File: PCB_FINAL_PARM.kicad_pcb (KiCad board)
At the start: 2 copper layers, 87.6 x 95.2 mm, 42 parts, among them J1 Conn_01x02_Servo1, J2 Conn_01x03_UART1, J3 Conn_01x03_UART2, J4 Conn_01x04_PWM, J5 Conn_01x05_PROGRAMER, J6 Conn_01x02_POWER, J7 Conn_01x02_Servo2, J8 Conn_01x02_Servo3, J9 Conn_01x02_Servo4, U2 DSPIC33EP128GM604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

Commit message: Proyecto Almost finalizado
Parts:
- added J10: Conn_01x04_TRIS, Connector_PinHeader_2.54mm:PinHeader_1x04_P2.54mm_Vertical, F.Cu at (209.4, 127.6)
- moved G*** 1.90 mm to (152.6, 63.3)
- moved C6 1.78 mm to (182.7, 117.8)
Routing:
- net Net-(J10-Pad1): track 0.00 -> 32.9 mm, vias 0 -> 1
- net Net-(J10-Pad2): track 0.00 -> 30.7 mm, vias 0 -> 1
- net Net-(J10-Pad3): track 0.00 -> 28.5 mm, vias 0 -> 1
- net Net-(J10-Pad4): track 0.00 -> 26.2 mm, vias 0 -> 1
- net Net-(J5-Pad5): track 51.0 -> 68.1 mm
- net Net-(J5-Pad4): track 64.9 -> 80.4 mm
- net GND: track 454.2 -> 455.6 mm
- net Net-(J4-Pad4): track 36.4 -> 37.8 mm
- net Net-(J4-Pad3): track 33.1 -> 34.1 mm
- net Net-(C3-Pad2): track 47.1 -> 46.4 mm
- net Net-(J4-Pad2): track 33.1 -> 33.7 mm
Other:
- board text added: "1"
- board text added: "2"
- board text added: "3"
- board text added: "3.3V"
- board text added: "4"
- board text added: "AUX"
- board text added: "M1"
- board text added: "M2"
- board text added: "M3"
- board text added: "P-ARM X Æ A-12"
- board text added: "RX"
- board text added: "TRIS PORT"
- board text added: "TX"
- board text removed: "P-ARM ALMOST"
- board text removed: "TM"

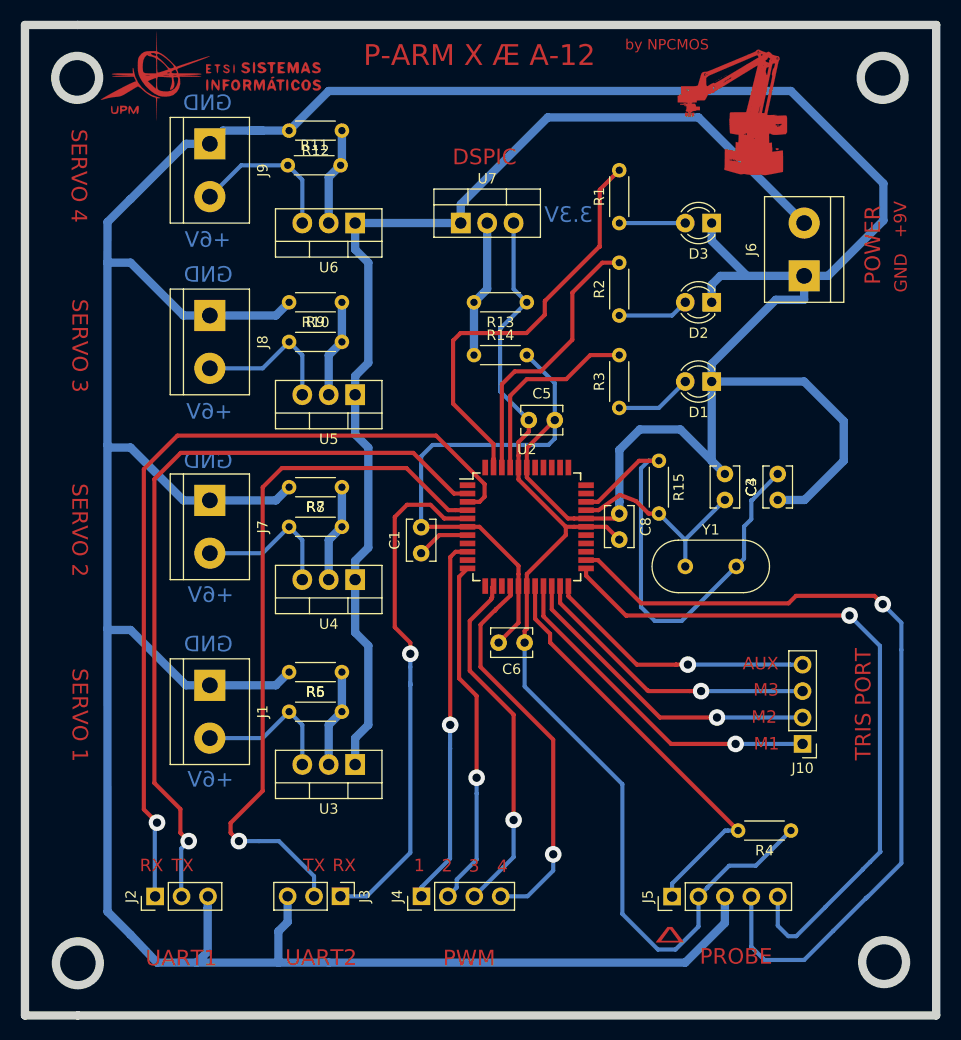
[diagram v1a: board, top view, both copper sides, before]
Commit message: Añadido puerto tris y clema extra
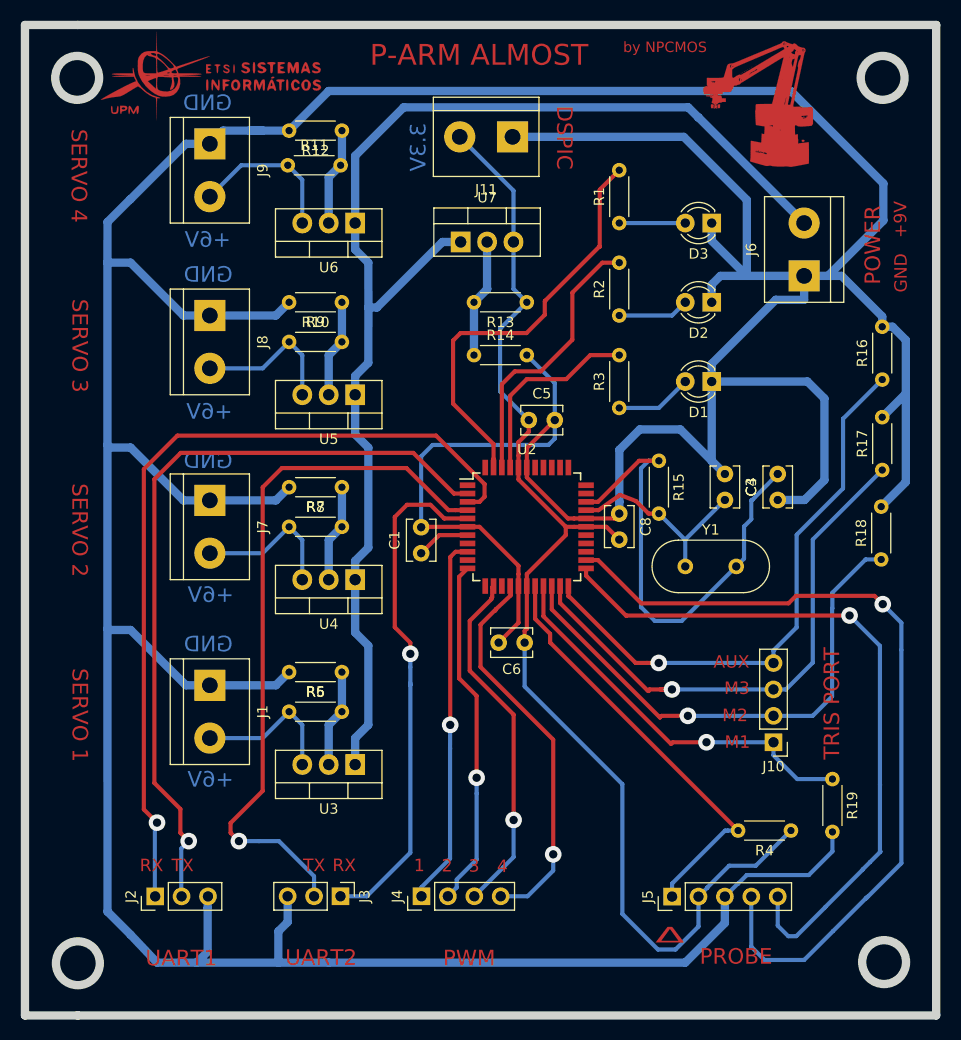
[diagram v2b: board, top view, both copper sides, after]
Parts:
- added J11: Conn_01x02_DSP, TerminalBlock:TerminalBlock_bornier-2_P5.08mm, F.Cu at (181.5, 69.2)
- added R16: 1k, Resistor_THT:R_Axial_DIN0204_L3.6mm_D1.6mm_P5.08mm_Horizontal, F.Cu at (217.1, 92.5)
- added R17: 1k, Resistor_THT:R_Axial_DIN0204_L3.6mm_D1.6mm_P5.08mm_Horizontal, F.Cu at (217.1, 101.2)
- added R18: 1k, Resistor_THT:R_Axial_DIN0204_L3.6mm_D1.6mm_P5.08mm_Horizontal, F.Cu at (217.0, 109.8)
- added R19: 1k, Resistor_THT:R_Axial_DIN0204_L3.6mm_D1.6mm_P5.08mm_Horizontal, F.Cu at (212.3, 130.9)
- moved J10 2.80 mm to (206.6, 127.4)
- moved G*** 2.62 mm to (205.2, 66.2)
- moved U7 1.82 mm to (176.5, 79.3)
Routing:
- net GND: track 455.6 -> 531.5 mm
- net Net-(J10-Pad4): track 26.2 -> 55.0 mm
- net Net-(J10-Pad3): track 28.5 -> 53.0 mm
- net Net-(J10-Pad2): track 30.7 -> 50.4 mm
- net Net-(J6-Pad2): track 107.9 -> 122.9 mm
- net +3V3: track 106.8 -> 117.2 mm
- net Net-(J10-Pad1): track 32.9 -> 38.4 mm
- net Net-(R13-Pad2): track 13.2 -> 11.4 mm
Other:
- board text added: "P-ARM ALMOST"
- board text removed: "P-ARM X Æ A-12"

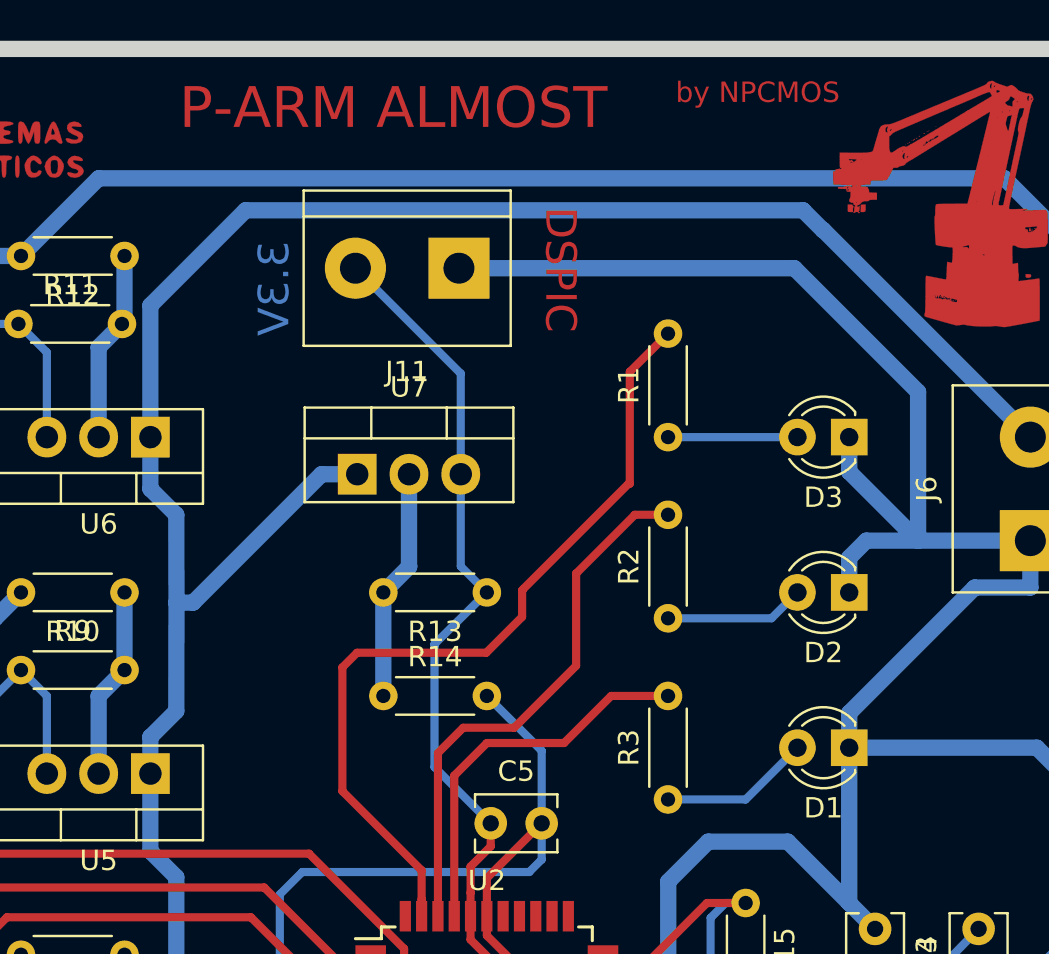
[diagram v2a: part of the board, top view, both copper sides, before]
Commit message: Añadido los circuitos de interruptores y sus pines de alimentación
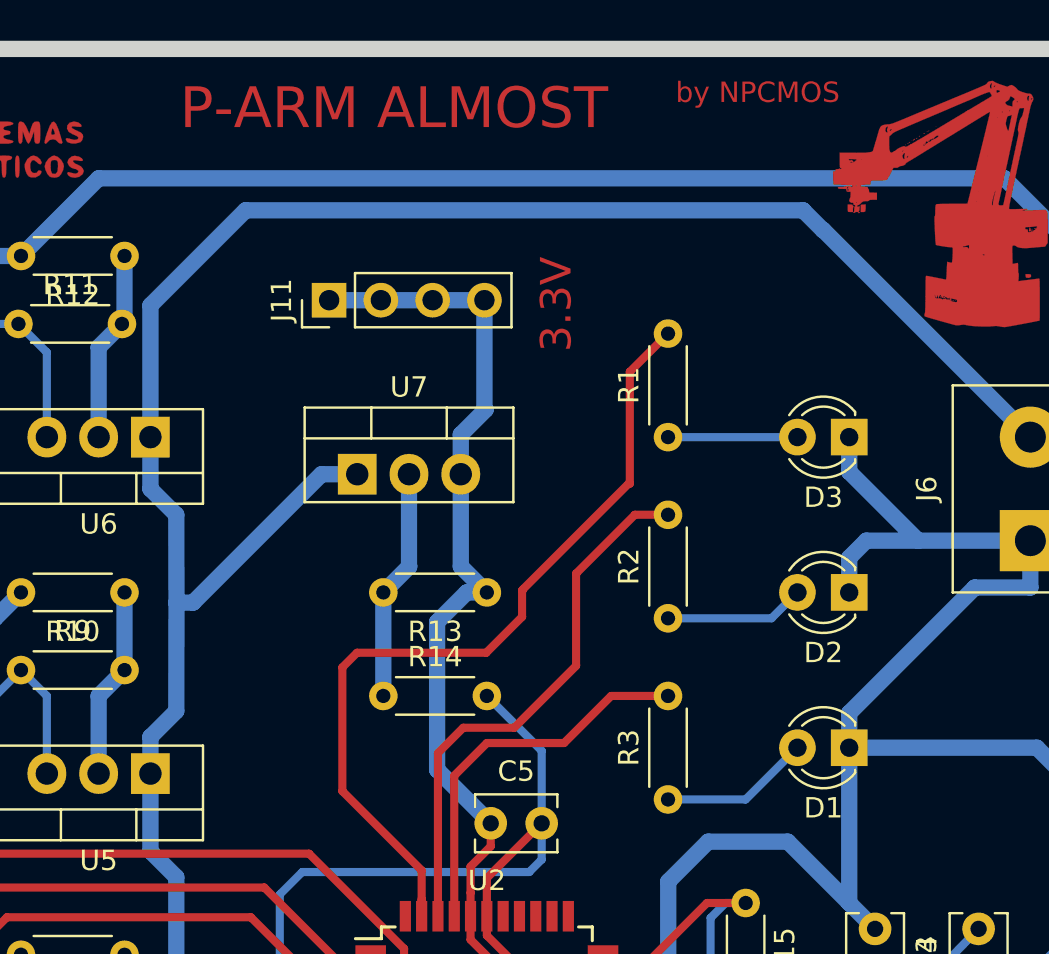
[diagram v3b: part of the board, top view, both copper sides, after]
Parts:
- J11: value Conn_01x02_DSP -> Conn_01x04_3v3; footprint TerminalBlock:TerminalBlock_bornier-2_P5.08mm -> Connector_PinHeader_2.54mm:PinHeader_1x04_P2.54mm_Vertical
- moved J11 6.56 mm to (175.1, 70.8), turned to 90 degrees
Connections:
- J11 pad 1: GND -> +3V3
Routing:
- net GND: track 531.5 -> 499.1 mm
- net +3V3: track 117.2 -> 122.1 mm
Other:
- board text removed: "DSPIC"
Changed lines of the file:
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@@
   (general
     (thickness 1.6)
-    (drawings 47)
-    (tracks 489)
+    (drawings 46)
+    (tracks 492)
     (zones 0)
     (modules 48)
@@
   )
   (setup
-    (last_trace_width 0.4)
+    (last_trace_width 0.8)
     (user_trace_width 0.4)
     (user_trace_width 0.8)
@@
     )
   )
-  (module TerminalBlock:TerminalBlock_bornier-2_P5.08mm (layer F.Cu)
-    (at 181.51 69.18 180)
-    (descr "simple 2-pin terminal block, pitch 5.08mm, revamped version of bornier2")
-    (tags "terminal block bornier2")
-    (fp_text reference J11 (at 2.54 -5.08) (layer F.SilkS)
-      (effects (font (size 1 1) (thickness 0.15)))
-    )
-    (fp_text value Conn_01x02_DSP (at 2.54 5.08) (layer F.Fab)
-      (effects (font (size 1 1) (thickness 0.15)))
-    )
-    (fp_text user %R (at 2.54 0) (layer F.Fab)
-      (effects (font (size 1 1) (thickness 0.15)))
-    )
-    (fp_line (start -2.41 2.55) (end 7.49 2.55) (layer F.Fab) (width 0.1))
-    (fp_line (start -2.46 -3.75) (end -2.46 3.75) (layer F.Fab) (width 0.1))
-    (fp_line (start -2.46 3.75) (end 7.54 3.75) (layer F.Fab) (width 0.1))
-    (fp_line (start 7.54 3.75) (end 7.54 -3.75) (layer F.Fab) (width 0.1))
-    (fp_line (start 7.54 -3.75) (end -2.46 -3.75) (layer F.Fab) (width 0.1))
-    (fp_line (start 7.62 2.54) (end -2.54 2.54) (layer F.SilkS) (width 0.12))
-    (fp_line (start 7.62 3.81) (end 7.62 -3.81) (layer F.SilkS) (width 0.12))
-    (fp_line (start 7.62 -3.81) (end -2.54 -3.81) (layer F.SilkS) (width 0.12))
-    (fp_line (start -2.54 -3.81) (end -2.54 3.81) (layer F.SilkS) (width 0.12))
-    (fp_line (start -2.54 3.81) (end 7.62 3.81) (layer F.SilkS) (width 0.12))
-    (fp_line (start -2.71 -4) (end 7.79 -4) (layer F.CrtYd) (width 0.05))
-    (fp_line (start -2.71 -4) (end -2.71 4) (layer F.CrtYd) (width 0.05))
-    (fp_line (start 7.79 4) (end 7.79 -4) (layer F.CrtYd) (width 0.05))
-    (fp_line (start 7.79 4) (end -2.71 4) (layer F.CrtYd) (width 0.05))
-    (pad 1 thru_hole rect (at 0 0 180) (size 3 3) (drill 1.52) (layers *.Cu *.Mask)
-      (net 2 GND))
-    (pad 2 thru_hole circle (at 5.08 0 180) (size 3 3) (drill 1.52) (layers *.Cu *.Mask)
-      (net 4 +3V3))
-    (model ${KISYS3DMOD}/TerminalBlock.3dshapes/TerminalBlock_bornier-2_P5.08mm.wrl
-      (offset (xyz 2.539999961853027 0 0))
-      (scale (xyz 1 1 1))
-      (rotate (xyz 0 0 0))
-    )
-  )
   (module Resistor_THT:R_Axial_DIN0204_L3.6mm_D1.6mm_P5.08mm_Horizontal (layer F.Cu)
     (at 217.06 92.52 90)
@@
     )
   )
+  (module Connector_PinHeader_2.54mm:PinHeader_1x04_P2.54mm_Vertical (layer F.Cu)
+    (at 175.14 70.75 90)
+    (descr "Through hole straight pin header, 1x04, 2.54mm pitch, single row")
+    (tags "Through hole pin header THT 1x04 2.54mm single row")
+    (fp_text reference J11 (at 0 -2.33 90) (layer F.SilkS)
+      (effects (font (size 1 1) (thickness 0.15)))
+    )
+    (fp_text value Conn_01x04_3v3 (at 0 9.95 90) (layer F.Fab)
+      (effects (font (size 1 1) (thickness 0.15)))
+    )
+    (fp_line (start -0.635 -1.27) (end 1.27 -1.27) (layer F.Fab) (width 0.1))
+    (fp_line (start 1.27 -1.27) (end 1.27 8.89) (layer F.Fab) (width 0.1))
+    (fp_line (start 1.27 8.89) (end -1.27 8.89) (layer F.Fab) (width 0.1))
+    (fp_line (start -1.27 8.89) (end -1.27 -0.635) (layer F.Fab) (width 0.1))
+    (fp_line (start -1.27 -0.635) (end -0.635 -1.27) (layer F.Fab) (width 0.1))
+    (fp_line (start -1.33 8.95) (end 1.33 8.95) (layer F.SilkS) (width 0.12))
+    (fp_line (start -1.33 1.27) (end -1.33 8.95) (layer F.SilkS) (width 0.12))
+    (fp_line (start 1.33 1.27) (end 1.33 8.95) (layer F.SilkS) (width 0.12))
+    (fp_line (start -1.33 1.27) (end 1.33 1.27) (layer F.SilkS) (width 0.12))
+    (fp_line (start -1.33 0) (end -1.33 -1.33) (layer F.SilkS) (width 0.12))
+    (fp_line (start -1.33 -1.33) (end 0 -1.33) (layer F.SilkS) (width 0.12))
+    (fp_line (start -1.8 -1.8) (end -1.8 9.4) (layer F.CrtYd) (width 0.05))
+    (fp_line (start -1.8 9.4) (end 1.8 9.4) (layer F.CrtYd) (width 0.05))
+    (fp_line (start 1.8 9.4) (end 1.8 -1.8) (layer F.CrtYd) (width 0.05))
+    (fp_line (start 1.8 -1.8) (end -1.8 -1.8) (layer F.CrtYd) (width 0.05))
+    (fp_text user %R (at 0 3.81) (layer F.Fab)
+      (effects (font (size 1 1) (thickness 0.15)))
+    )
+    (pad 1 thru_hole rect (at 0 0 90) (size 1.7 1.7) (drill 1) (layers *.Cu *.Mask)
+      (net 4 +3V3))
+    (pad 2 thru_hole oval (at 0 2.54 90) (size 1.7 1.7) (drill 1) (layers *.Cu *.Mask)
+      (net 4 +3V3))
+    (pad 3 thru_hole oval (at 0 5.08 90) (size 1.7 1.7) (drill 1) (layers *.Cu *.Mask)
+      (net 4 +3V3))
+    (pad 4 thru_hole oval (at 0 7.62 90) (size 1.7 1.7) (drill 1) (layers *.Cu *.Mask)
+      (net 4 +3V3))
+    (model ${KISYS3DMOD}/Connector_PinHeader_2.54mm.3dshapes/PinHeader_1x04_P2.54mm_Vertical.wrl
+      (at (xyz 0 0 0))
+      (scale (xyz 1 1 1))
+      (rotate (xyz 0 0 0))
+    )
+  )
+  (gr_text "3.3V\n" (at 186.29 70.95 90) (layer F.Cu)
+    (effects (font (size 1.5 1.5) (thickness 0.3)))
+  )
   (gr_text "TRIS PORT\n" (at 212.22 123.66 90) (layer F.Cu)
     (effects (font (size 1.5 1.5) (thickness 0.3)))
@@
     (effects (font (size 1.2 1.2) (thickness 0.3)))
   )
-  (gr_text 3.3V (at 172.44 70.17 90) (layer B.Cu)
-    (effects (font (size 1.5 1.5) (thickness 0.3)) (justify mirror))
-  )
   (gr_text 4 (at 180.53 139.33) (layer F.Cu)
     (effects (font (size 1.2 1.2) (thickness 0.3)))
@@
   (gr_circle (center 217.24 148.54) (end 219.349502 148.54) (layer Edge.Cuts) (width 0.8))
   (gr_circle (center 217.1 63.509502) (end 219.209502 63.509502) (layer Edge.Cuts) (width 0.8))
-  (gr_text DSPIC (at 186.49 69.25 270) (layer F.Cu)
-    (effects (font (size 1.5 1.5) (thickness 0.3)))
-  )
   (gr_text "SERVO 1" (at 139.89 124.78 270) (layer F.Cu)
     (effects (font (size 1.5 1.5) (thickness 0.3)))
@@
     (effects (font (size 1 1) (thickness 0.125)))
   )
-  (gr_text "P-ARM ALMOST\n\n\n\n" (at 178.29 66.15) (layer F.Cu)
+  (gr_text "P-ARM ALMOST\n\n\n\n" (at 178.32 66.16) (layer F.Cu)
     (effects (font (size 2 2) (thickness 0.3)))
   )
@@
   (segment (start 182.08 115.91) (end 180.17 117.82) (width 0.4) (layer F.Cu) (net 2))
   (segment (start 182.08 112.38) (end 182.08 115.91) (width 0.4) (layer F.Cu) (net 2))
-  (segment (start 181.51 69.18) (end 197.97 69.18) (width 0.8) (layer B.Cu) (net 2))
-  (segment (start 204.04 75.25) (end 204.04 82.55) (width 0.8) (layer B.Cu) (net 2))
-  (segment (start 197.97 69.18) (end 204.04 75.25) (width 0.8) (layer B.Cu) (net 2))
   (segment (start 211.5 102.19) (end 209.59 104.1) (width 0.8) (layer B.Cu) (net 2))
   (segment (start 211.5 94.34) (end 211.5 102.19) (width 0.8) (layer B.Cu) (net 2))
@@
   (segment (start 200.239999 141.390001) (end 200.239999 141.370001) (width 0.4) (layer B.Cu) (net 4))
   (segment (start 200.239999 141.370001) (end 202.34 139.27) (width 0.4) (layer B.Cu) (net 4))
-  (segment (start 183.07 96.42) (end 180.31 93.66) (width 0.4) (layer B.Cu) (net 4))
-  (segment (start 180.31 93.66) (end 180.31 87.63) (width 0.4) (layer B.Cu) (net 4))
-  (segment (start 182.88 85.09) (end 180.31 87.63) (width 0.4) (layer B.Cu) (net 4))
   (segment (start 180.31 87.63) (end 180.34 87.63) (width 0.4) (layer B.Cu) (net 4))
   (segment (start 182.08 99.83) (end 182.08 100.98) (width 0.4) (layer F.Cu) (net 4))
@@
   (segment (start 182.67 122.03) (end 182.67 117.82) (width 0.4) (layer B.Cu) (net 4))
   (segment (start 192.07 131.43) (end 182.67 122.03) (width 0.4) (layer B.Cu) (net 4))
-  (segment (start 181.6 83.81) (end 181.6 79.29) (width 0.4) (layer B.Cu) (net 4))
-  (segment (start 182.88 85.09) (end 181.6 83.81) (width 0.4) (layer B.Cu) (net 4))
-  (segment (start 181.6 74.35) (end 181.6 79.29) (width 0.4) (layer B.Cu) (net 4))
-  (segment (start 176.43 69.18) (end 181.6 74.35) (width 0.4) (layer B.Cu) (net 4))
+  (segment (start 181.6 83.81) (end 182.88 85.09) (width 0.8) (layer B.Cu) (net 4))
+  (segment (start 181.6 79.29) (end 181.6 83.81) (width 0.8) (layer B.Cu) (net 4))
+  (segment (start 181.890051 85.09) (end 180.44 86.540051) (width 0.8) (layer B.Cu) (net 4))
+  (segment (start 182.88 85.09) (end 181.890051 85.09) (width 0.8) (layer B.Cu) (net 4))
+  (segment (start 180.44 93.79) (end 183.07 96.42) (width 0.8) (layer B.Cu) (net 4))
+  (segment (start 180.44 86.540051) (end 180.44 93.79) (width 0.8) (layer B.Cu) (net 4))
+  (segment (start 181.6 79.29) (end 181.6 77.34) (width 0.8) (layer B.Cu) (net 4))
+  (segment (start 181.6 77.34) (end 182.82 76.12) (width 0.8) (layer B.Cu) (net 4))
+  (segment (start 182.76 76.06) (end 182.76 70.75) (width 0.8) (layer B.Cu) (net 4))
+  (segment (start 182.82 76.12) (end 182.76 76.06) (width 0.8) (layer B.Cu) (net 4))
+  (segment (start 180.22 70.75) (end 182.76 70.75) (width 0.8) (layer B.Cu) (net 4))
+  (segment (start 177.68 70.75) (end 180.22 70.75) (width 0.8) (layer B.Cu) (net 4))
+  (segment (start 175.14 70.75) (end 177.68 70.75) (width 0.8) (layer B.Cu) (net 4))
   (segment (start 195.58 95.25) (end 198.12 92.71) (width 0.4) (layer B.Cu) (net 5))
   (segment (start 191.77 95.25) (end 195.58 95.25) (width 0.4) (layer B.Cu) (net 5))

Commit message: Revisada la posición del cristal y engrosadas algunas pistas
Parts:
- moved C3 6.27 mm to (202.5, 99.7)
- moved Y1 5.90 mm to (197.6, 104.6), turned to 90 degrees
- moved C4 2.99 mm to (202.6, 104.5)
- moved R15 2.56 mm to (193.1, 99.7)
- moved C8 2.01 mm to (192.6, 107.2)
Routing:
- net Net-(C3-Pad2): track 46.4 -> 18.5 mm
- net GND: track 499.1 -> 485.7 mm
- net Net-(C4-Pad2): track 19.6 -> 15.2 mm
- net +3V3: track 122.1 -> 123.8 mm
